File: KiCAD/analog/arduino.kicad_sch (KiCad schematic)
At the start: 48 parts, among them J12 Screw_Terminal_01x04, J13 Screw_Terminal_01x03, J14 Screw_Terminal_01x05, J17 Conn_Coaxial_Small, J18 Conn_Coaxial_Small, J19 Conn_Coaxial_Small, J2 8P8C_Shielded, J20 Screw_Terminal_01x04, J21 Screw_Terminal_01x02, J22 Screw_Terminal_01x04, J23 Conn_Coaxial_Small, J24 Conn_Coaxial_Small, J29 Conn_Coaxial_Small, J3 Screw_Terminal_01x04, J30 Conn_Coaxial_Small, J31 8P8C_Shielded, J32 Screw_Terminal_01x02, J6 Screw_Terminal_01x02, J7 Screw_Terminal_01x02, J8 Screw_Terminal_01x02, J9 Screw_Terminal_01x02, Q10 2N7000, Q4 2N7000, Q5 2N7000, Q6 2N7000, Q7 2N7000, U17 Adafruit_PCF8575_Breakout, U18 CD14538B, U3 MCP4728

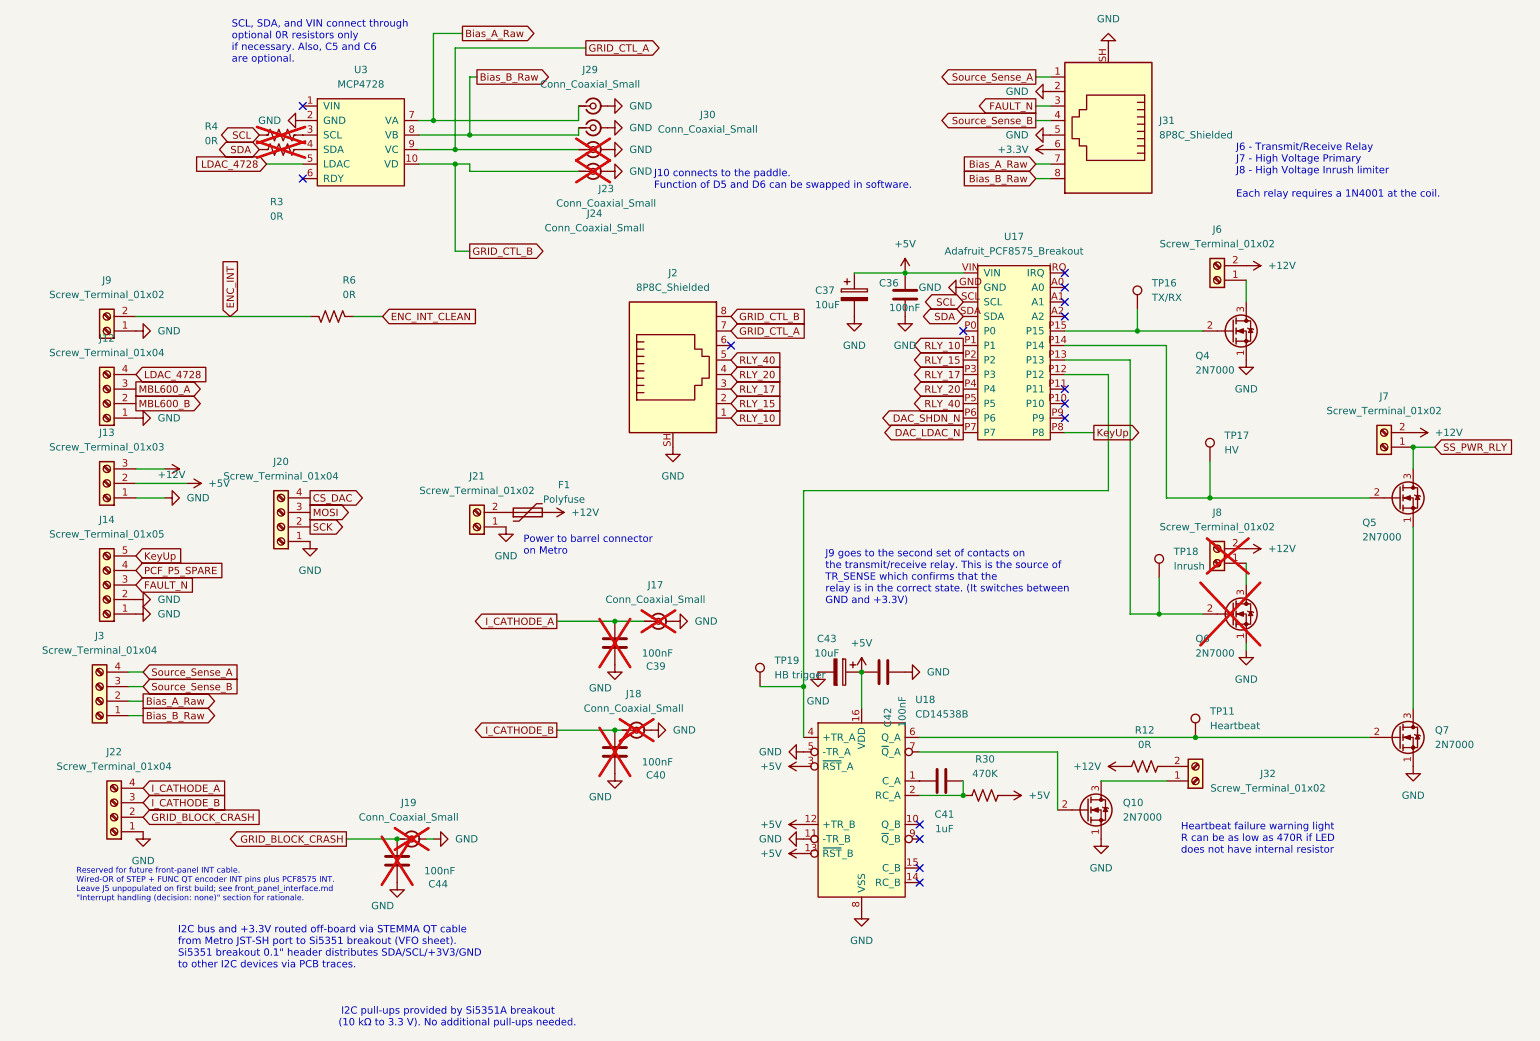
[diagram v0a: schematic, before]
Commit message: revD: DGFET-DAC bias scheme, kit-style xfmr naming, custom footprints, Output LPF project
Architecture refinements since the previous revD commit (f8d7058):

Analog board (vfo_complete, arduino, dac, power sheets):
  * MCP4922 (U4) ch B exposed as DRIVER_BIAS DAC output -> J31 pin 6
    (replaces the +3.3V pin that was on J31 pin 6 before). Analog's U4
    now controls the ss_pa BS170 driver DC bias point directly from
    firmware -- cleaner than the kit's trimmer+Q201 scheme.
  * MCP4728 (U3) ch A/B exposed as PA_Bias_A_Raw / PA_Bias_B_Raw ->
    J31 pins 7, 8. These feed the ss_pa CD74HC4066 fault-switch (U2),
    which gates them to PA_Bias_A/B on the IRF510 gates. On FAULT_N
    low, switch opens -> IRF510 bias collapses -> conduction cuts.
  * Rename pass: Bias_A/B/_Raw labels -> PA_Bias_A/B/_Raw everywhere
    (analog J3 screw-terminal, umbilical J31, ss_pa U2 inputs). Prefix
    disambiguates from DRIVER_BIAS which drives a different stage.
  * J2 (band-select RJ45 to Output LPF board): added RLY_40 provision.
    Pin layout reorganized -- RLY_40 lives at pin 5, pin 6 kept as a
    spare for a future 6th band.

ss_pa board (pa_stage, fault_shutdown, lpf sheets):
  * Driver + final BS170/IRF510 topology drawn following QRP Labs
    10W Linear kit (RF IN -> T201 input xfmr -> BS170 PP driver
    (Q2, Q6) -> T202 interstage -> IRF510 PP finals (Q3, Q4) ->
    T203 bifilar drain feed -> T204 output xfmr -> RF out).
  * Transformer references renamed to match the kit: T201 (input,
    BN61-2402), T202 (interstage, BN61-2402), T203 (drain feed,
    T50-43), T204 (output, BN43-202).
  * Driver bias filter on DRIVER_BIAS: C19 (0.1uF) + C20 (100pF)
    bulk + HF bypass, into T201 secondary CT (pin 4).
  * +3.3V now locally regulated on ss_pa (MCP1700x-330xxTO, U13)
    from +13.8V, powering U1 (LM393) and U2 (CD74HC4066). J31
    pin 6 freed up for DRIVER_BIAS.
  * Duplicate RJ45 J7 deleted (was a leftover from pre-DAC-bias era).
  * J3 (SMA RF input from analog) foo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
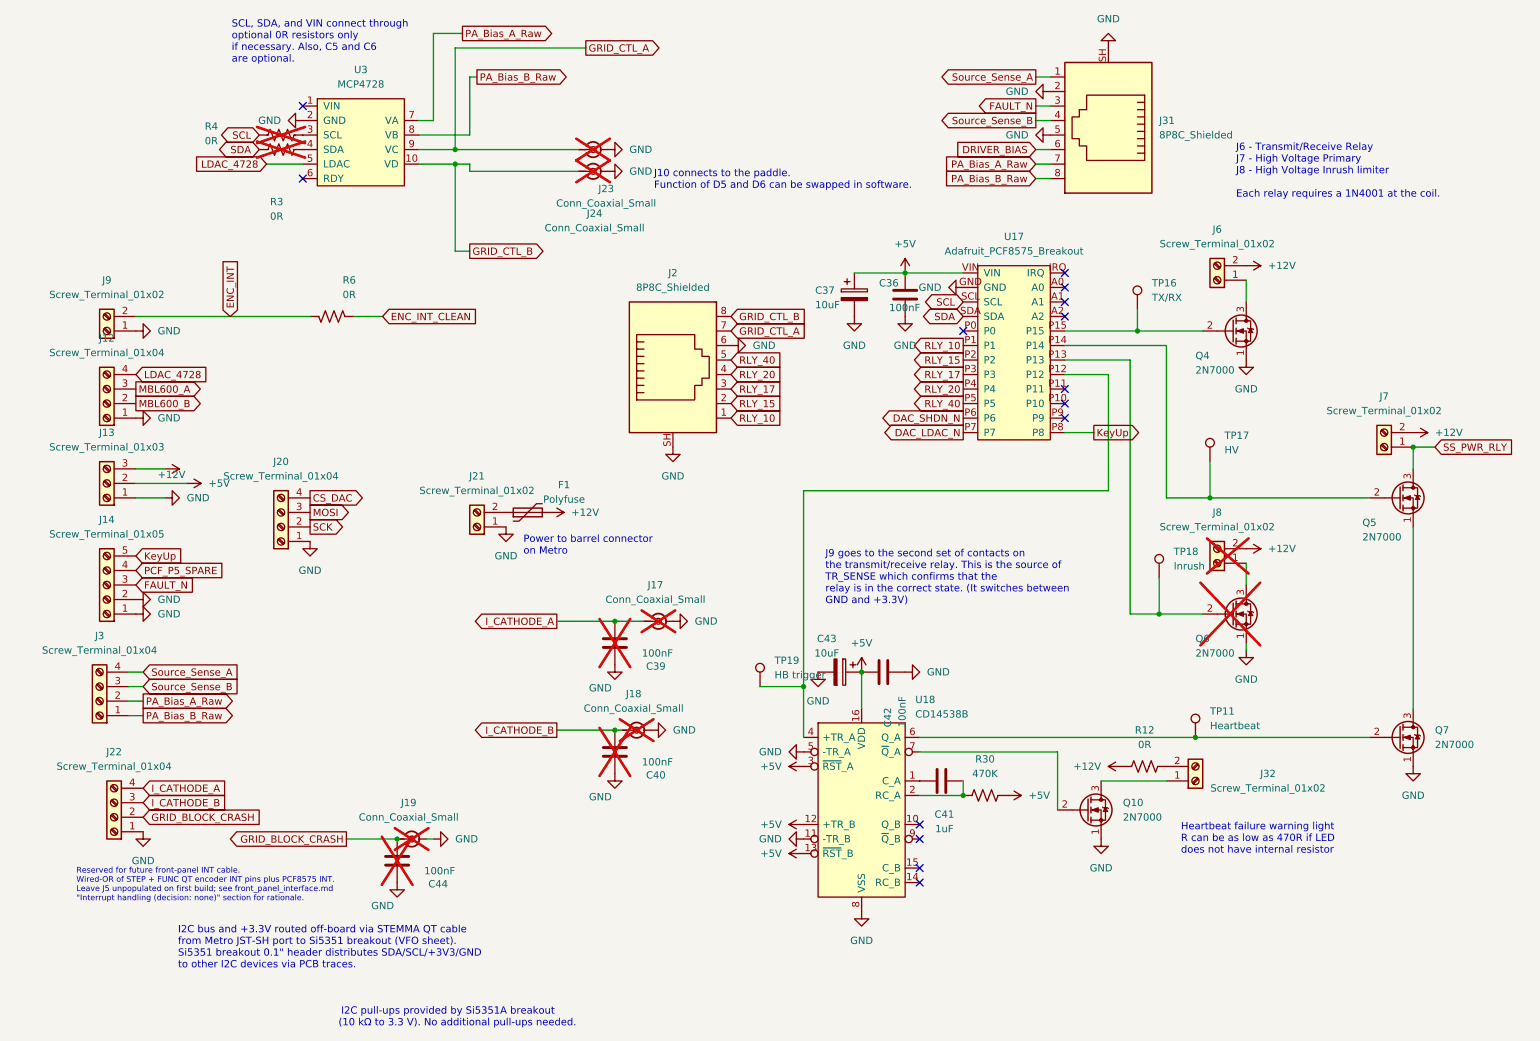
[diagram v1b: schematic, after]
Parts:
- removed J29, J30: Conn_Coaxial_Small, xmitter:SMA_Cinch_142-0701-201_Vertical_JackPCB, symbol Connector:Conn_Coaxial_Small
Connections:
- net GND: now also J2.6
- net +3.3V renamed DRIVER_BIAS
- net Bias_A_Raw renamed PA_Bias_A_Raw
- net Bias_B_Raw renamed PA_Bias_B_Raw
- no-connect marks 15 -> 14

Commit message: revD analog: consolidate all tube-PA control signals onto new J35 RJ45
Added J35 (Amphenol RJE1D-188 RJ45) on the analog arduino sheet as
a dedicated single-connector umbilical for every signal needed to
drive a future tube-PA upgrade. Replaces the scattered SMA jacks
and the stop-gap "GRID_CTL squatting on J2 pins 7, 8" arrangement.

Signals now on J35 (T568B pair layout):
  pin 1  I_CATHODE_A        (future tube A cathode sense -> Metro ADC)
  pin 2  GND
  pin 3  I_CATHODE_B        (future tube B cathode sense)
  pin 4  GRID_CTL_A         (MCP4728 U3 ch C -> future tube A grid bias)
  pin 5  GRID_CTL_B         (MCP4728 U3 ch D -> future tube B grid bias)
  pin 6  GND
  pin 7  GND
  pin 8  GRID_BLOCK_CRASH   (fault signal -> future bias crash)
  SH     GND

Side effects on other analog connectors:
  * J2 (LPF umbilical) pins 7, 8 freed up: GRID_CTL_A/B moved off
    J2 and onto J35. J2 is now purely band-select (RLY_10/15/17/20/40
    on pins 1-5, GND on pin 6, pins 7/8 unconnected spares).
  * J22 (4-pin screw terminal) and J23/J24 (SMAs) retained as
    intentional bench/scope-probe access to the same tube control
    signals -- parallel paths to J35, not duplicate-wiring errors.

Docs updated:
  * Documentation/revD_interconnect.md
  * Documentation/Master_Description.md

Co-Authored-By: Claude Opus 4.7 <noreply@anthropic.com>
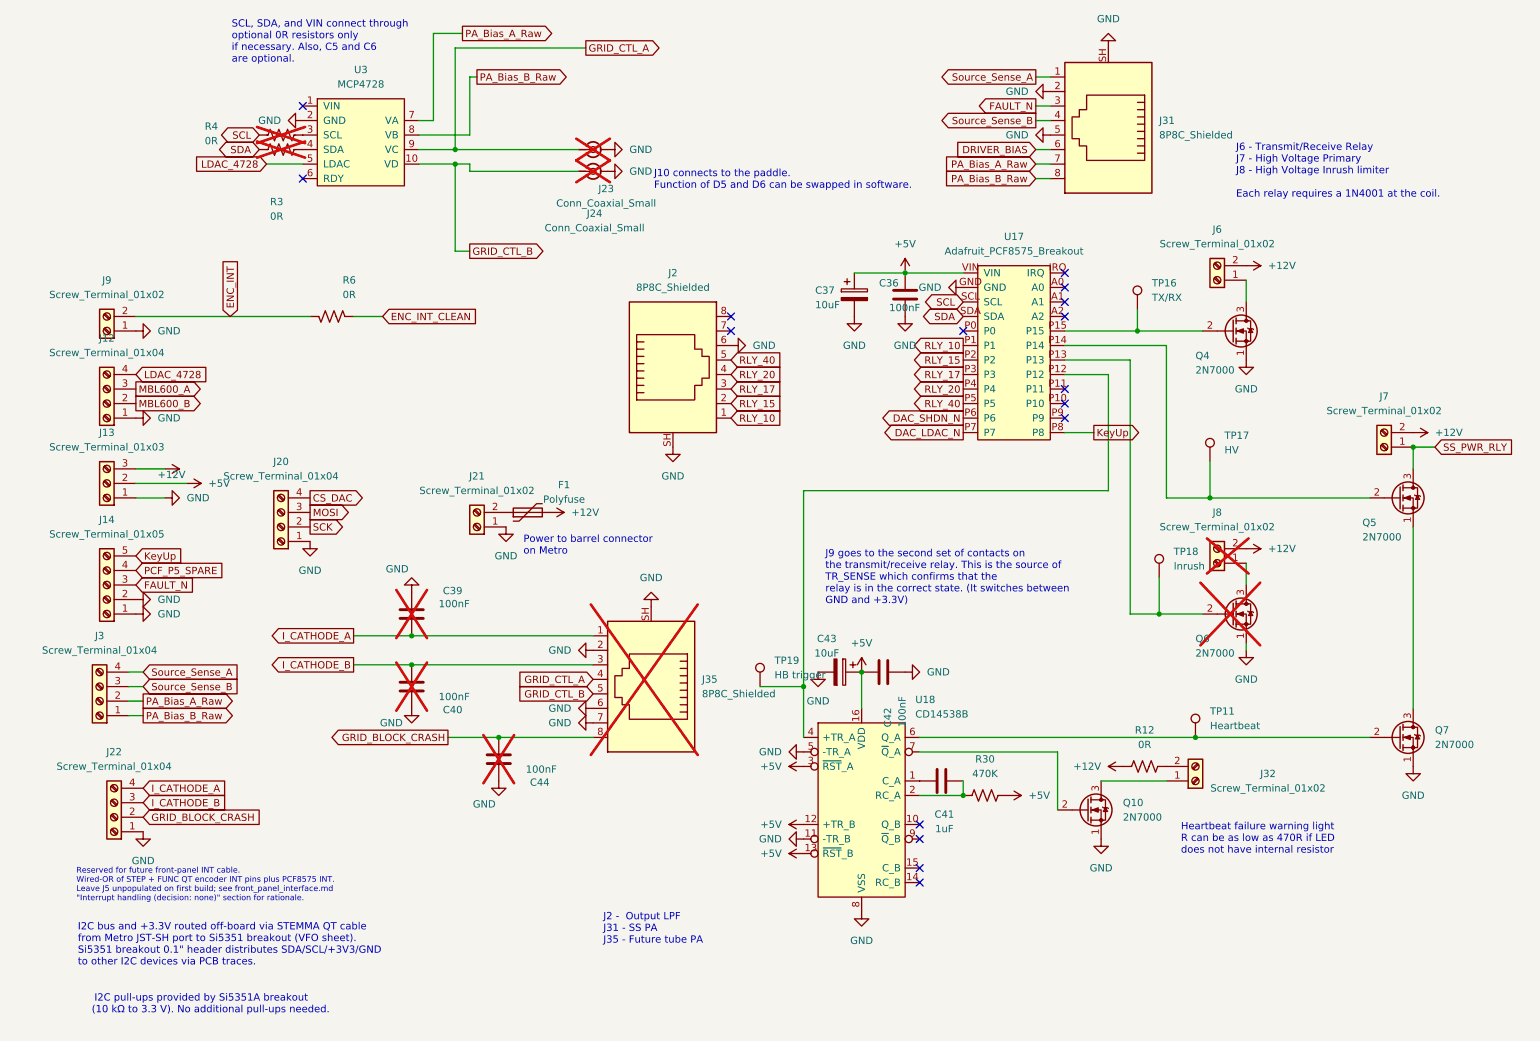
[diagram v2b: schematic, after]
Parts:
- removed J17, J18, J19: Conn_Coaxial_Small, xmitter:SMA_Cinch_142-0701-201_Vertical_JackPCB, symbol Connector:Conn_Coaxial_Small
- added J35: 8P8C_Shielded, xmitter:Amphenol_RJE1D-188_Horizontal_Shielded, symbol Connector:8P8C_Shielded
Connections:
- net GND: now also J35.2, J35.6, J35.7, J35.SH
- net GRID_BLOCK_CRASH: now also J35.8
- net GRID_CTL_A: now also J35.4; no longer J2.7
- net GRID_CTL_B: now also J35.5; no longer J2.8
- net I_CATHODE_A: now also J35.1
- net I_CATHODE_B: now also J35.3
- no-connect marks 14 -> 16
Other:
- note added: "J2 - Output LPF J31 - SS PA J35 - Future tube PA"
- moved on the sheet: C39, C40, C44

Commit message: revD analog: J23/J24 SMAs removed, many test points added, test_points.md
Schematic cleanup round:
  * Deleted J23 and J24 (SMAs that had carried GRID_CTL_A/B).
    These were redundant now that J35 is the production tube-PA
    control umbilical. Bench probing of GRID_CTL_A/B is now via
    TP2/TP1 (test-point pads) instead of SMA jacks.
  * Added 21 test points (TP1..TP21) across arduino, dac, and
    vfo_complete sheets. Covers:
      - Tube-PA control bus (TP1,2,5,6,7)
      - SS PA bias/sense/fault (TP3,4,12,13,14,15)
      - Keyer / envelope / U1 output (TP10,20,21)
      - DAC control lines (TP8,9)
      - Relay driver gates (TP11,16,17,18)
      - Hardware watchdog trigger (TP19)
    All on standard test-point pads for scope-probe or DMM access.

New doc: Documentation/test_points.md
  * Grouped TP table by functional area
  * Includes source/description for each signal
  * Includes a "how to use at the bench" section with common
    debug workflows (RF chain, bias setting, fault chain,
    future tube-PA bring-up, watchdog verification)
  * Uses monospace-aligned columns rather than markdown tables,
    per project convention for saved docs

Co-Authored-By: Claude Opus 4.7 <noreply@anthropic.com>
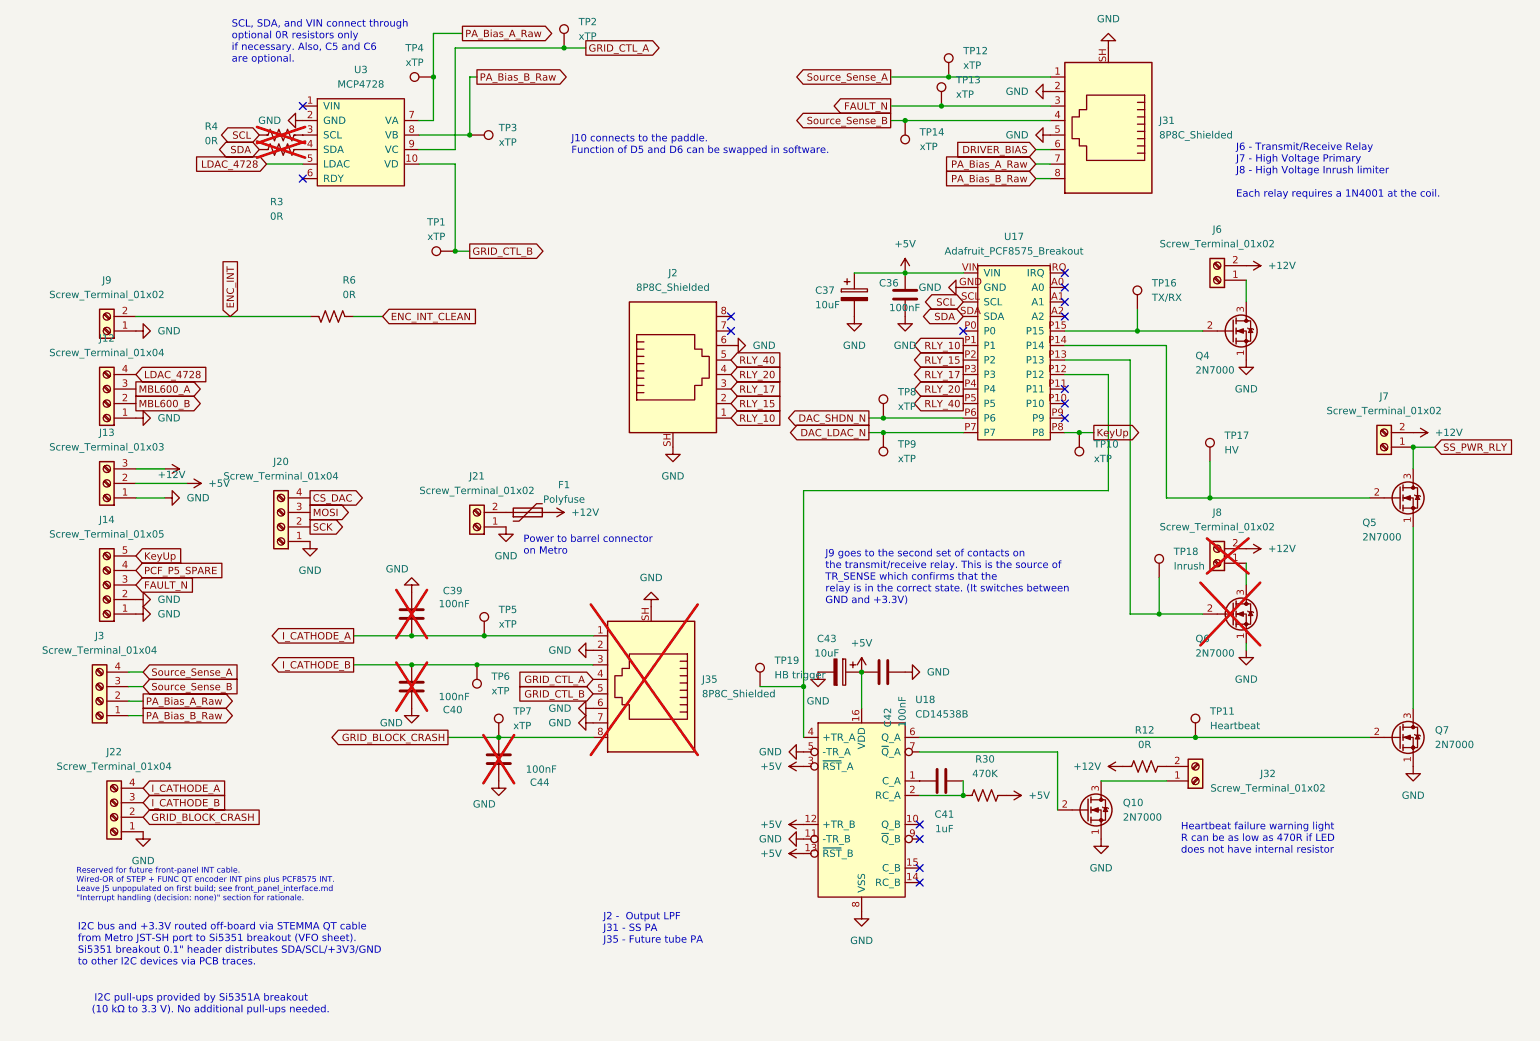
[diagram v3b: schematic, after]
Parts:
- removed J23, J24: Conn_Coaxial_Small, xmitter:SMA_Cinch_142-0701-201_Vertical_JackPCB, symbol Connector:Conn_Coaxial_Small
- added TP1, TP10, TP12, TP13, TP14, TP2, TP3, TP4, TP5, TP6, TP7, TP8, TP9: xTP, Connector_PinHeader_2.54mm:PinHeader_1x01_P2.54mm_Vertical, symbol xmitter:xTP
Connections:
- net DAC_LDAC_N: now also TP9.1
- net DAC_SHDN_N: now also TP8.1
- net FAULT_N: now also TP13.1
- net GRID_BLOCK_CRASH: now also TP7.1
- net GRID_CTL_A: now also TP2.1
- net GRID_CTL_B: now also TP1.1
- net I_CATHODE_A: now also TP5.1
- net I_CATHODE_B: now also TP6.1
- net KeyUp: now also TP10.1
- net PA_Bias_A_Raw: now also TP4.1
- net PA_Bias_B_Raw: now also TP3.1
- net Source_Sense_A: now also TP12.1
- net Source_Sense_B: now also TP14.1
